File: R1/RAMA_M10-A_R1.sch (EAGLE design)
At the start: 40 parts, among them Q2 PCHANNEL-MOSFET, Y1 16MHz

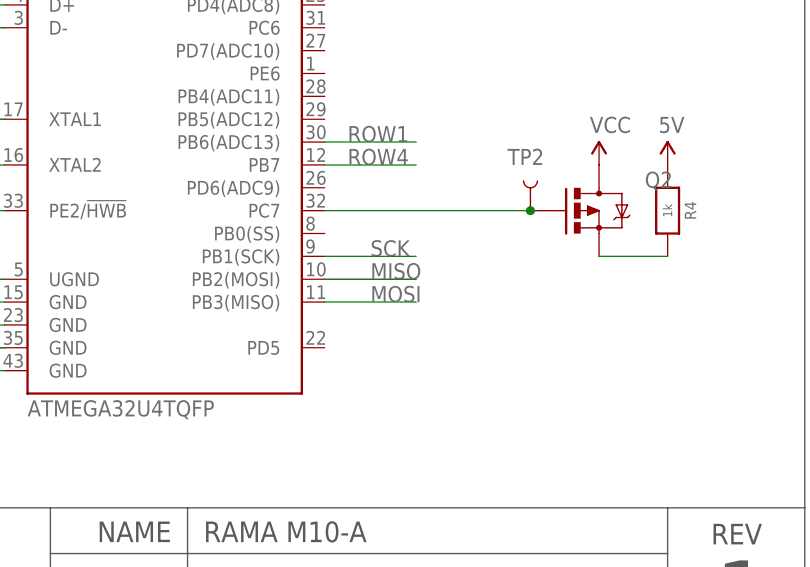
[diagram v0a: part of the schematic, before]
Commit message: Rounded corners, strengthened mounting holes, changed fonts to nicer hand-drawn font, altered USB & TQFN-44 footprints, fixed incorrectly reversed MISO/MOSI, altered copper pour on RAMA & Machine logos
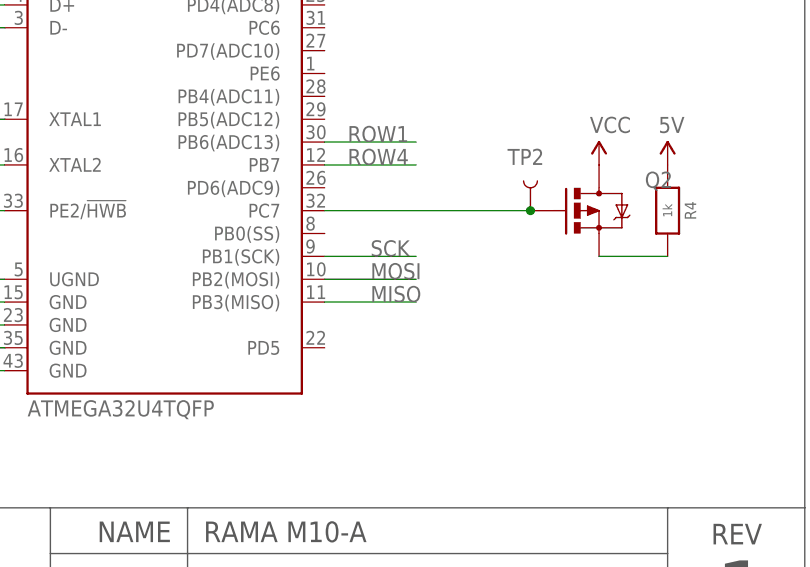
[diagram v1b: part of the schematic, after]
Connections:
- net MISO: now also U$8.PB3(MISO); no longer U$8.PB2(MOSI)
- net MOSI: now also U$8.PB2(MOSI); no longer U$8.PB3(MISO)
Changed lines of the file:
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@@
 <net name="MOSI" class="0">
+<segment>
+<pinref part="ISP1" gate="G$1" pin="MOSI"/>
+<wire x1="363.22" y1="144.78" x2="370.84" y2="144.78" width="0.1524" layer="91"/>
+<label x="363.22" y="144.78" size="1.778" layer="95"/>
+</segment>
+<segment>
+<pinref part="U$8" gate="G$1" pin="PB2(MOSI)"/>
+<wire x1="325.12" y1="40.64" x2="335.28" y2="40.64" width="0.1524" layer="91"/>
+<label x="330.2" y="40.64" size="1.778" layer="95"/>
+</segment>
+</net>
+<net name="MISO" class="0">
+<segment>
+<pinref part="ISP1" gate="G$1" pin="MISO"/>
+<wire x1="335.28" y1="147.32" x2="327.66" y2="147.32" width="0.1524" layer="91"/>
+<label x="327.66" y="147.32" size="1.778" layer="95"/>
+</segment>
 <segment>
 <pinref part="U$8" gate="G$1" pin="PB3(MISO)"/>
@@
 <label x="330.2" y="38.1" size="1.778" layer="95"/>
 </segment>
-<segment>
-<pinref part="ISP1" gate="G$1" pin="MOSI"/>
-<wire x1="363.22" y1="144.78" x2="370.84" y2="144.78" width="0.1524" layer="91"/>
-<label x="363.22" y="144.78" size="1.778" layer="95"/>
-</segment>
 </net>
-<net name="MISO" class="0">
-<segment>
-<pinref part="U$8" gate="G$1" pin="PB2(MOSI)"/>
-<wire x1="325.12" y1="40.64" x2="335.28" y2="40.64" width="0.1524" layer="91"/>
-<label x="330.2" y="40.64" size="1.778" layer="95"/>
-</segment>
-<segment>
-<pinref part="ISP1" gate="G$1" pin="MISO"/>
-<wire x1="335.28" y1="147.32" x2="327.66" y2="147.32" width="0.1524" layer="91"/>
-<label x="327.66" y="147.32" size="1.778" layer="95"/>
-</segment>
-</net>

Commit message: Pre-prod
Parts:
- removed R4: 1k, Adafruit Bluefruit LE nRF8001:RESISTOR_0603MP
- added ISP2: AVRISP-SMT, adafruit:AVRISP-SMT
- added JP1: (no value), SparkFun-Connectors:M06SIP
- added R10, R11, R12, R13, R14, R15, R16, R7, R8, R9: 100ohm, Adafruit Bluefruit LE nRF8001:RESISTOR_0603MP
- added R6: 10k, Adafruit Bluefruit LE nRF8001:RESISTOR_0603MP
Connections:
- removed net N$4: Q2.S, R4.2
- new net JP_GND: ISP2.GND, JP1.6
- new net JP_MISO: ISP2.MISO, JP1.1
- new net JP_RST: ISP2.RST, JP1.3
- new net JP_SCK: ISP2.SCK, JP1.2
- new net JP_VCC: ISP2.VCC, JP1.4
- new net N$28: KEY7.LED2, R13.2
- new net N$29: KEY8.LED2, R14.2
- new net N$30: KEY9.LED2, R15.2
- new net N$31: KEY10.LED2, R16.2
- new net N$32: KEY4.LED2, R10.2
- new net N$69: KEY5.LED2, R11.2
- new net N$70: KEY6.LED2, R12.2
- new net N$71: KEY3.LED2, R9.2
- new net N$72: KEY2.LED2, R8.2
- new net N$73: KEY1.LED2, R7.2
- new net N$74: ISP2.MOSI, JP1.5
- net 5V: now also Q2.D; no longer R4.1
- net GND: now also R10.1, R11.1, R12.1, R13.1, R14.1, R15.1, R16.1, R7.1, R8.1, R9.1; no longer KEY1.LED2, KEY10.LED2, KEY2.LED2, KEY3.LED2, KEY4.LED2, KEY5.LED2, KEY6.LED2, KEY7.LED2, KEY8.LED2, KEY9.LED2
- net N$13: now also R6.2
- net VCC: now also Q2.S, R6.1; no longer Q2.D
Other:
- moved on the sheet: Q2, TP2
